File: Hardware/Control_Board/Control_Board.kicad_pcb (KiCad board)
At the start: 2 copper layers, 129.5 x 130.8 mm, 18 parts, among them J2 Term_01x02, J22 Conn_02x20_Odd_Even, J7 Term_01x02, K2 ALQ3F12

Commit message: PCB layout additions
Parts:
- added J**: 172447-YY02, Samacsys:172447-YY02, F.Cu at (45.7, 48.3)
- added J**: 172447-YY02, Samacsys:172447-YY02, F.Cu at (45.7, 55.9)
- added J**: 172447-YY02, Samacsys:172447-YY02, F.Cu at (45.7, 71.1)
- added J**: 172447-YY02, Samacsys:172447-YY02, F.Cu at (45.7, 63.5)
- D2 (x4): value LED -> LED_Red_power
- J2: value Term_01x02 -> Screw_Terminal_01x02
- R5 (x4): value 2k -> 10k
- moved D2 29.2 mm to (123.4, 124.4)
- moved J2 29.2 mm to (151.8, 141.6)
- moved J7 29.2 mm to (151.8, 127.6)
- moved J7 29.2 mm to (152.2, 88.9)
- moved K2 29.2 mm to (125.7, 128.9)
- moved K2 29.2 mm to (126.1, 102.9)
- moved R5 29.2 mm to (123.4, 108.0)
- moved K2 29.2 mm to (126.1, 90.2)
- moved D2 29.2 mm to (123.4, 111.1)
- moved D2 29.2 mm to (123.9, 85.7)
- moved D2 29.2 mm to (123.9, 98.4)
- moved J7 29.2 mm to (152.2, 101.6)
- moved J7 29.2 mm to (151.8, 114.3)
- moved K2 29.2 mm to (125.7, 115.6)
- moved R5 29.2 mm to (123.9, 95.2)
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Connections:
- D2 pad 1: (no net) -> Net-(D2-Pad1) (x4)
- D2 pad 2: (no net) -> +5V (x4)
- J2 pad 1: (no net) -> +12V
- J2 pad 2: (no net) -> +12V
- J7 pad 1: (no net) -> Net-(J7-Pad1) (x4)
- J7 pad 2: (no net) -> Net-(J7-Pad1) (x4)
- K2 pad 1: (no net) -> 12V (x4)
- K2 pad 2: (no net) -> Relay2 (x4)
- K2 pad 3: (no net) -> Net-(J5-Pad1) (x4)
- K2 pad 4: (no net) -> 120V_Hot (x4)
- R5 pad 1: (no net) -> GND (x4)
- R5 pad 2: (no net) -> Net-(R4-Pad1) (x4)
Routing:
- net (no net): track 12.8 -> 2.63 mm
- net GND: track 0.00 -> 8.65 mm
- net Net-(R4-Pad1): track 0.00 -> 1.56 mm
- added copper zone on B.Cu, net 120V_Hot
- added copper zone on F.Cu, net 120V_Hot
- added copper zone on B.Cu, net Net-(J7-Pad1)
- added copper zone on F.Cu, net Net-(J7-Pad1)
- removed copper zone on B.Cu, net (none)
- removed copper zone on F.Cu, net (none)
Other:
- outline, holes or cut-outs redrawn

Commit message: Control_Board updates
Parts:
- removed the D2 at (123.4, 111.1)
- removed the D2 at (123.9, 85.7)
- removed the D2 at (123.4, 124.4)
- removed the D2 at (123.9, 98.4)
- removed J** (x4): 172447-YY02, Samacsys:172447-YY02
- removed J22: Conn_02x20_Odd_Even, Connector_PinSocket_2.54mm:PinSocket_2x20_P2.54mm_Vertical
- removed the R5 at (123.4, 108.0)
- removed the R5 at (123.9, 95.2)
- removed the R5 at (123.4, 121.3)
- removed the R5 at (123.9, 82.5)
- added A1: Arduino_Nano_v3.x, Module:Arduino_Nano, F.Cu at (47.0, 78.7)
- added C1: 10uF, Capacitor_SMD:C_1206_3216Metric, F.Cu at (203.4, 63.2)
- added C2: 10uF, Capacitor_SMD:C_1206_3216Metric, F.Cu at (207.5, 61.7)
- added C3: 100nF, Capacitor_SMD:C_0603_1608Metric, F.Cu at (203.4, 57.7)
- added C4: 22uF, Capacitor_SMD:C_1206_3216Metric, F.Cu at (211.8, 55.4)
- added C5: 22uF, Capacitor_SMD:C_1206_3216Metric, F.Cu at (211.8, 53.0)
- added D1: LED_Red_power, LED_SMD:LED_0603_1608Metric, F.Cu at (195.8, 55.7)
- added D2: LED_Red_power, LED_SMD:LED_0603_1608Metric, F.Cu at (211.3, 63.0)
- added J1: Raspberry_Pi_2_3, Library Loader:HDRV40W64P254_2X20_5080X500X884P, F.Cu at (89.2, 75.2)
- added J7: 12V PWR IN, 1792863-2term_power:1792863, F.Cu at (44.2, 44.5)
- added L1: 3.3uH, Inductor_SMD:L_10.4x10.4_H4.8, F.Cu at (203.5, 49.0)
- added Q1: PMOS, Package_SO:SOIC-8_3.9x4.9mm_P1.27mm, F.Cu at (196.7, 59.3)
- added Q2: Q_Dual_PMOS_S1G1S2G2D2D2D1D1, Package_SO:SOP-8_3.9x4.9mm_P1.27mm, F.Cu at (212.6, 59.4)
- added R1: 10k, Resistor_SMD:R_0402_1005Metric_Pad0.72x0.64mm_HandSolder, F.Cu at (44.7, 76.9)
- added R2: 20k, Resistor_SMD:R_0402_1005Metric_Pad0.72x0.64mm_HandSolder, F.Cu at (43.9, 78.7)
- added R3: 10k, Resistor_SMD:R_0402_1005Metric, F.Cu at (198.4, 55.6)
- added R4: 56.2k, Resistor_SMD:R_0402_1005Metric, F.Cu at (208.0, 56.1)
- added R5: 10k, Resistor_SMD:R_0402_1005Metric, F.Cu at (208.0, 58.2)
- added R6: 6.8k, Resistor_SMD:R_0402_1005Metric, F.Cu at (214.1, 63.0)
- added R7: 6.8k, Resistor_SMD:R_0402_1005Metric, F.Cu at (214.1, 64.0)
- added U1: ULN2003, Package_SO:SOIC-16_3.9x9.9mm_P1.27mm, F.Cu at (116.8, 102.9)
- added U2: ULN2003, Package_SO:SOIC-16_3.9x9.9mm_P1.27mm, F.Cu at (118.1, 66.0)
- added U3: TPS563200, Package_TO_SOT_SMD:SOT-23-6, F.Cu at (203.3, 60.3)
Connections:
- K2 pad 1: 12V -> +12V (x4)
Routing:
- net U2/Pin1: track 0.00 -> 69.6 mm
- net U2/Pin3: track 0.00 -> 45.4 mm
- net Relay2: track 0.00 -> 44.0 mm
- net U2/Pin4: track 0.00 -> 42.8 mm
- net U2/Pin2: track 0.00 -> 38.0 mm
- net U1/Pin3: track 0.00 -> 33.5 mm, vias 0 -> 1
- net U1/Pin4: track 0.00 -> 33.2 mm, vias 0 -> 1
- net U1/Pin1: track 0.00 -> 23.9 mm, vias 0 -> 1
- net U1/Pin2: track 0.00 -> 23.0 mm, vias 0 -> 1
- net Relay1: track 0.00 -> 19.9 mm
- net GND: track 8.65 -> 0.00 mm
- net (no net): track 2.63 -> 0.00 mm
- net Net-(R4-Pad1): track 1.56 -> 0.00 mm
- added copper zone on F.Cu, net +12V
- added copper zone on B.Cu, net GND
- removed copper zone on F.Cu, net 120V_Hot
- removed copper zone on F.Cu, net Net-(J7-Pad1)
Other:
- outline, holes or cut-outs redrawn
- board text removed: "Relay 2"

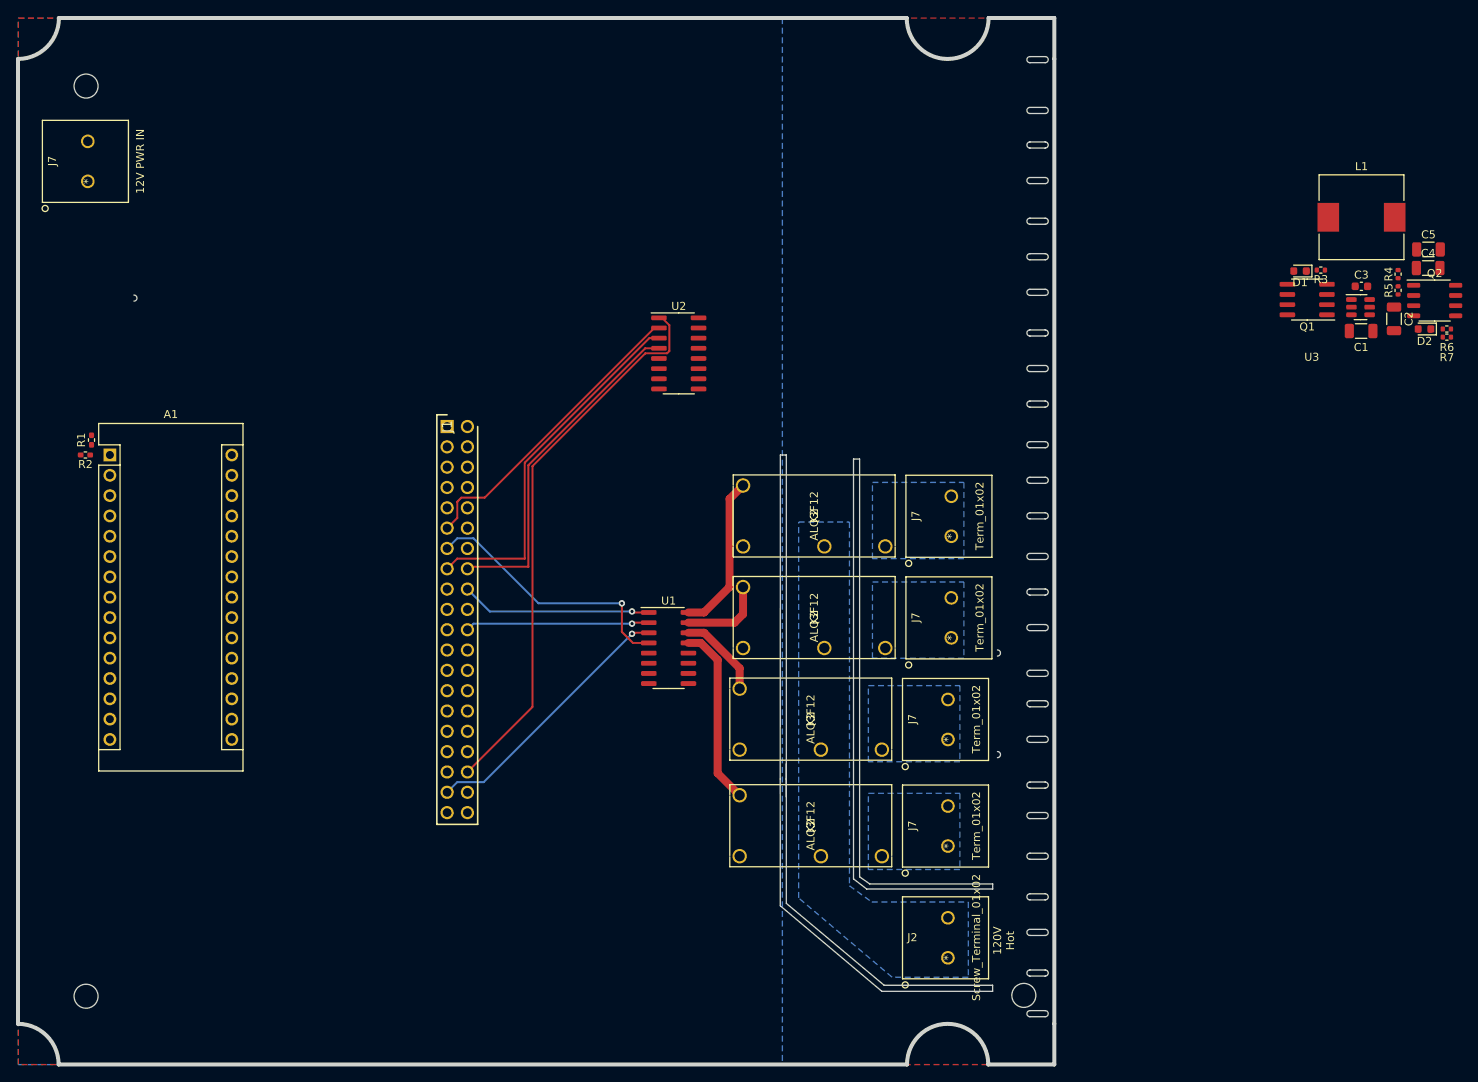
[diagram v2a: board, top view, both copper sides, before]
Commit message: Board updates, ready for power regulation component placements
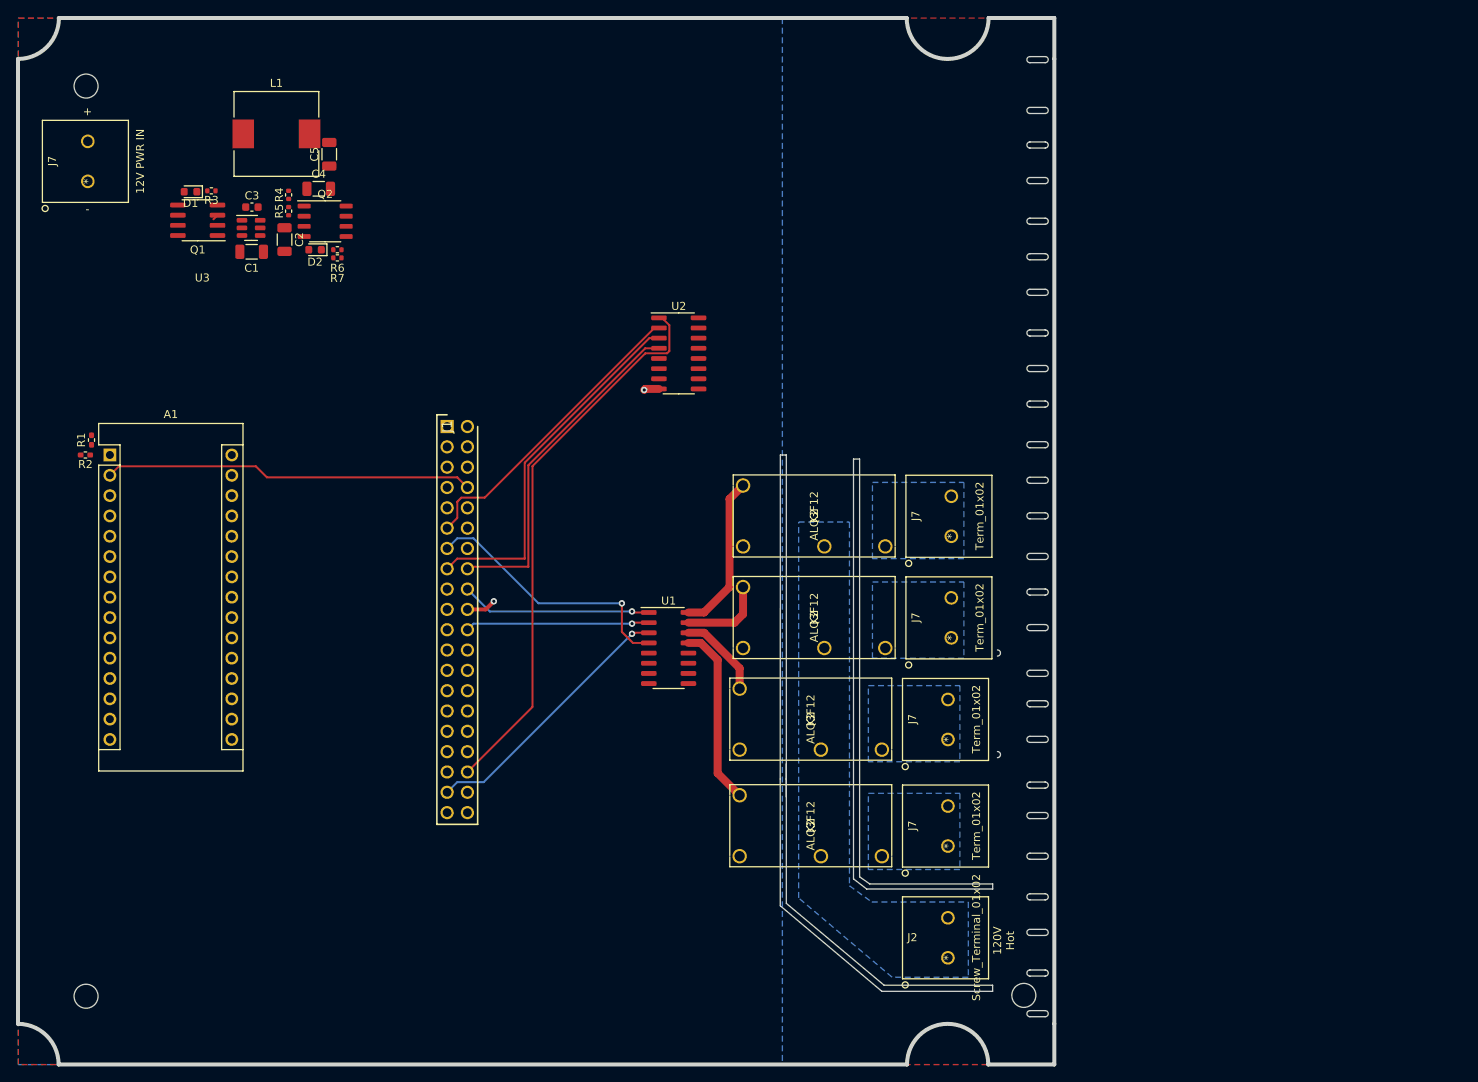
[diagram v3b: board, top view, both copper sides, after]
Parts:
- moved C4 139.0 mm to (73.1, 45.5)
- moved Q2 139.0 mm to (73.9, 49.5)
- moved R4 139.0 mm to (69.3, 46.2)
- moved R5 139.0 mm to (69.3, 48.3)
- moved R6 139.0 mm to (75.4, 53.1)
- moved R7 139.0 mm to (75.4, 54.1)
- moved U3 139.0 mm to (64.6, 50.4)
- moved C1 139.0 mm to (64.7, 53.3)
- moved C2 139.0 mm to (68.8, 51.8)
- moved C3 139.0 mm to (64.8, 47.8)
- moved D1 139.0 mm to (57.1, 45.8)
- moved D2 139.0 mm to (72.6, 53.1)
- moved Q1 139.0 mm to (58.0, 49.4)
- moved R3 139.0 mm to (59.7, 45.7)
- moved C5 137.9 mm to (74.4, 41.1), turned to 90 degrees
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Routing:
- net TX: track 0.00 -> 46.3 mm
- net GND: track 0.00 -> 5.62 mm, vias 0 -> 2
- net Net-(C1-Pad1): track 0.00 -> 0.72 mm
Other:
- outline, holes or cut-outs redrawn
- board text added: "+"
- board text added: "-"

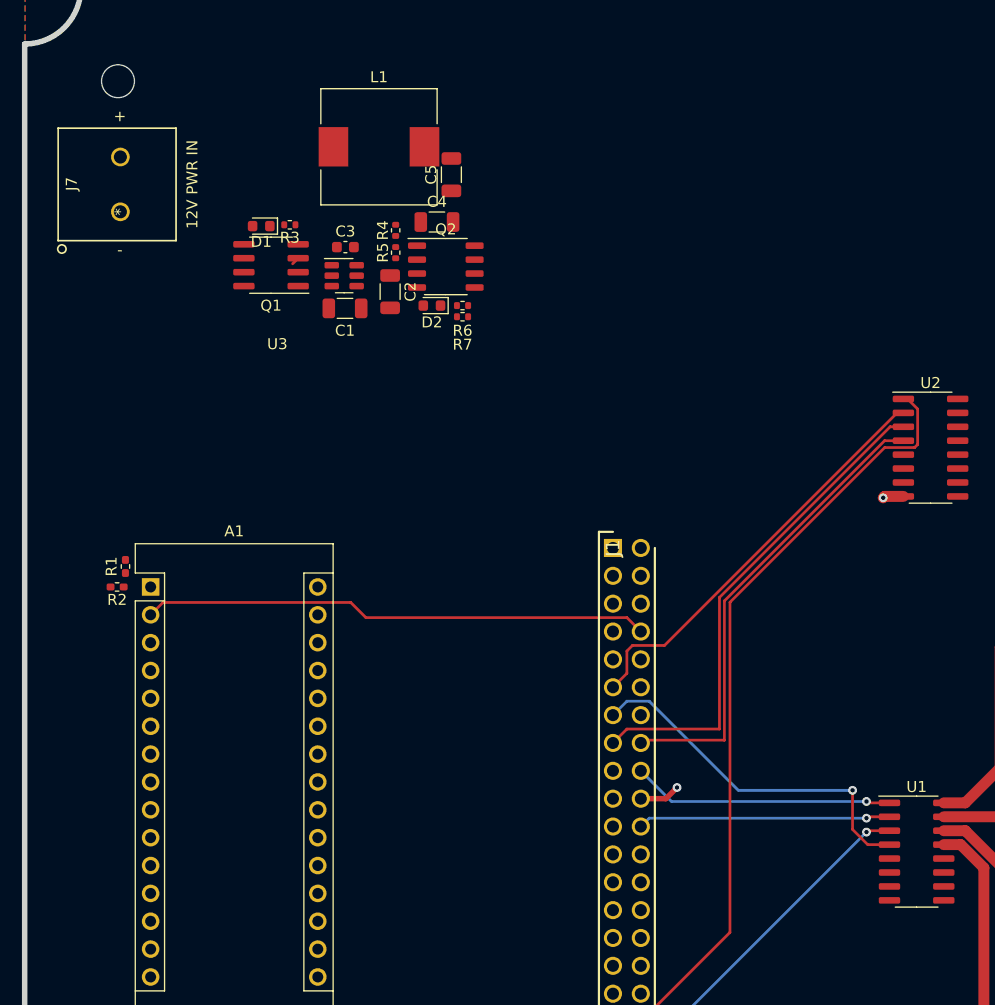
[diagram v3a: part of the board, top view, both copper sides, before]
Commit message: Laid out power regulation stuffs
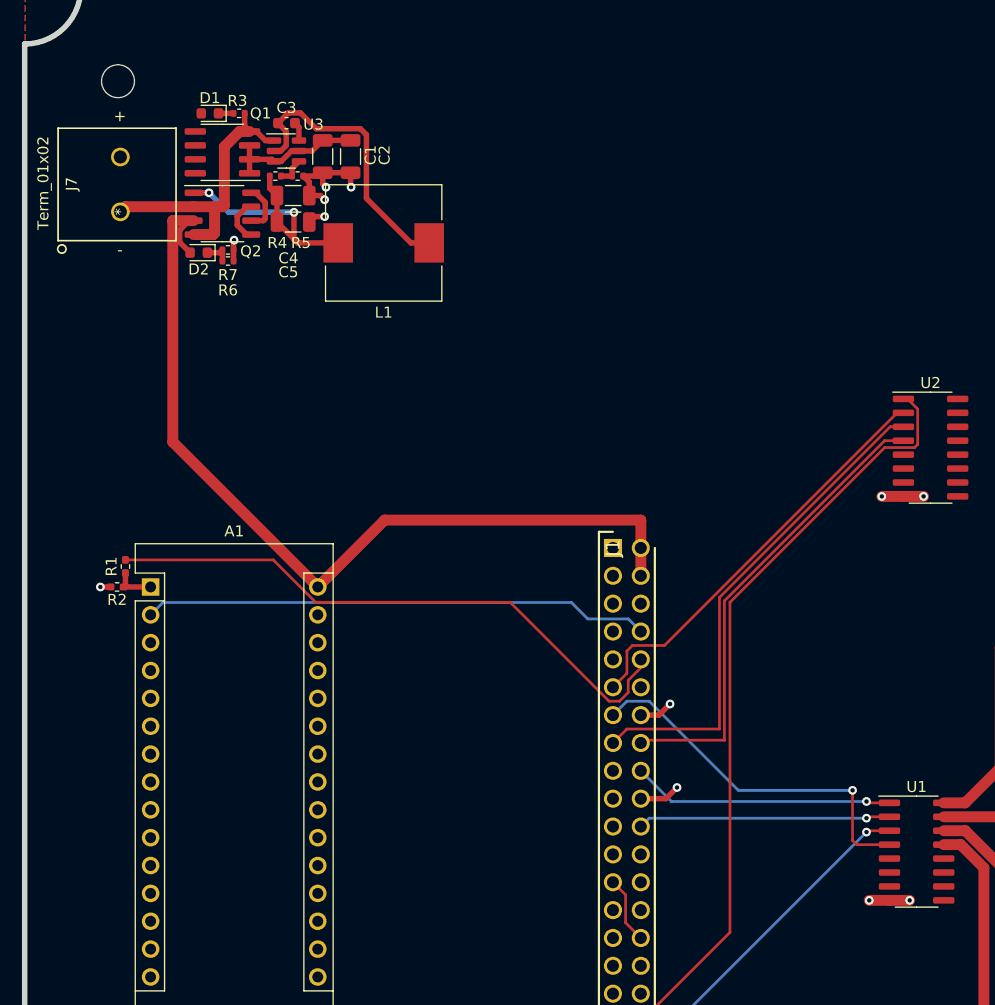
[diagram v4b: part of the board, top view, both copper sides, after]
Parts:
- J7: value 12V PWR IN -> Term_01x02
- moved R7 22.2 mm to (54.1, 48.0)
- moved D2 21.8 mm to (51.4, 48.3)
- moved R6 21.8 mm to (54.1, 49.0)
- moved Q2 20.9 mm to (53.5, 44.7)
- moved C5 15.1 mm to (60.0, 45.5), turned to 0 degrees
- moved C1 14.0 mm to (62.7, 39.5), turned to -90 degrees
- moved C4 13.3 mm to (60.0, 43.1)
- moved C2 12.8 mm to (65.2, 39.5)
- moved U3 12.5 mm to (59.4, 39.0)
- moved C3 12.5 mm to (59.4, 36.4)
- moved R4 12.0 mm to (58.4, 41.3), turned to 180 degrees
- moved R5 11.3 mm to (60.4, 41.3), turned to 180 degrees
- moved D1 11.3 mm to (52.4, 35.6)
- moved Q1 11.2 mm to (53.5, 39.1)
- moved R3 11.2 mm to (55.1, 35.6)
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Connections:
- J7 pad 1: GND -> Net-(J7-Pad1)
- J7 pad 2: +12V -> Net-(J7-Pad1)
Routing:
- net +5V: track 0.00 -> 81.9 mm
- net GND: track 5.62 -> 62.4 mm, vias 2 -> 12
- net Net-(J1-Pad10): track 0.00 -> 55.0 mm
- net Net-(C3-Pad1): track 0.00 -> 26.1 mm
- net Net-(C4-Pad1): track 0.00 -> 23.7 mm, vias 0 -> 2
- net Relay2: track 44.0 -> 63.9 mm
- net Relay1: track 19.9 -> 0.00 mm
- net Net-(C1-Pad1): track 0.72 -> 12.6 mm
- net Net-(Q2-Pad6): track 0.00 -> 4.48 mm
- net Net-(Q2-Pad5): track 0.00 -> 4.08 mm
- net RX: track 0.00 -> 3.80 mm
- net Net-(R4-Pad1): track 0.00 -> 2.61 mm
- net Net-(D2-Pad1): track 0.00 -> 2.49 mm
- net Net-(C3-Pad2): track 0.00 -> 1.74 mm
- net Net-(D1-Pad1): track 0.00 -> 1.37 mm
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
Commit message: 10_23_2022_3_pin_headers
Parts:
- added A0: HDRV3W64P0X254_1X3_762X254X864P, Library:HDRV3W64P0X254_1X3_762X254X864P, F.Cu at (67.9, 110.6)
- added A1: HDRV3W64P0X254_1X3_762X254X864P, Library:HDRV3W64P0X254_1X3_762X254X864P, F.Cu at (67.9, 105.0)
- added A2: HDRV3W64P0X254_1X3_762X254X864P, Library:HDRV3W64P0X254_1X3_762X254X864P, F.Cu at (67.7, 99.1)
- added A3: HDRV3W64P0X254_1X3_762X254X864P, Library:HDRV3W64P0X254_1X3_762X254X864P, F.Cu at (67.7, 93.3)
- added A4: HDRV3W64P0X254_1X3_762X254X864P, Library:HDRV3W64P0X254_1X3_762X254X864P, F.Cu at (67.4, 87.4)
- added T/H: HDRV3W64P0X254_1X3_762X254X864P, Library:HDRV3W64P0X254_1X3_762X254X864P, F.Cu at (80.1, 76.5)
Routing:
- net +5V: track 81.9 -> 193.2 mm
- net Net-(J1-Pad10): track 55.0 -> 41.5 mm
- net A4: track 0.00 -> 12.3 mm
- net A0: track 0.00 -> 11.1 mm
- net A3: track 0.00 -> 10.4 mm
- net A1: track 0.00 -> 9.57 mm
- net unconnected-(J1-Pad7): track 0.00 -> 9.13 mm
- net A2: track 0.00 -> 9.04 mm
- net GND: track 62.4 -> 64.0 mm
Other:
- board text added: "5V"
- board text added: "GND"
- board text added: "GPIO4"
- board text added: "S"

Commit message: Updated Analog sensor routing
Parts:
- moved T/H 14.1 mm to (72.1, 64.8)
- moved A4 3.02 mm to (68.6, 90.2)
- moved A3 2.10 mm to (68.6, 95.2)
- moved A2 1.55 mm to (68.6, 100.3)
- moved A1 0.74 mm to (68.6, 105.4)
- moved A0 0.65 mm to (68.6, 110.5)
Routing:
- net +5V: track 193.2 -> 124.7 mm
- net Relay2: track 63.9 -> 10.7 mm
- net Net-(J1-Pad10): track 41.5 -> 56.9 mm, vias 0 -> 1
- net unconnected-(J1-Pad7): track 9.13 -> 24.3 mm
- net GND: track 64.0 -> 55.5 mm
- net A2: track 9.04 -> 10.3 mm
- net A1: track 9.57 -> 10.8 mm
- net A3: track 10.4 -> 11.1 mm
- net TX: track 46.3 -> 47.0 mm
- net A4: track 12.3 -> 13.0 mm
- net A0: track 11.1 -> 11.7 mm

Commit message: v0.1 Ready for review
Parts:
- removed J7 (x5): Term_01x02, 1792863-2term_power:1792863
- removed the K2 at (125.7, 128.9)
- removed the K2 at (126.1, 102.9)
- removed the K2 at (126.1, 90.2)
- removed the K2 at (125.7, 115.6)
- added J**: 197054301, Samacsys:197054301, F.Cu at (139.7, 64.8)
- added J**: 197054301, Samacsys:197054301, F.Cu at (152.1, 58.4)
- added J**: 197054301, Samacsys:197054301, F.Cu at (139.7, 52.1)
- added J**: 197054301, Samacsys:197054301, F.Cu at (152.1, 71.1)
- added J**: 197054301, Samacsys:197054301, F.Cu at (152.1, 64.8)
- added J**: 197054301, Samacsys:197054301, F.Cu at (139.7, 58.4)
- added J**: 197054301, Samacsys:197054301, F.Cu at (152.1, 52.1)
- added J**: 197054301, Samacsys:197054301, F.Cu at (139.7, 71.1)
- added J112: 19705-4301, Samacsys:197054301, F.Cu at (151.1, 128.3)
- added J3: Screw_Terminal_01x02, Samacsys:197054301, F.Cu at (40.6, 45.1)
- added J4: 19705-4301, Samacsys:197054301, F.Cu at (151.8, 89.5)
- added J5: 19705-4301, Samacsys:197054301, F.Cu at (151.1, 101.6)
- added J6: 19705-4301, Samacsys:197054301, F.Cu at (151.1, 114.9)
- added J8: 19705-4301, Samacsys:197054301, F.Cu at (151.1, 141.6)
- added K1: ALQ3F12, Samacsys:G5Q1A4DC24, F.Cu at (126.2, 90.3)
- added K2: ALQ3F12, Samacsys:G5Q1A4DC24, F.Cu at (126.2, 103.0)
- added K3: ALQ3F12, Samacsys:G5Q1A4DC24, F.Cu at (126.2, 115.7)
- added K4: ALQ3F12, Samacsys:G5Q1A4DC24, F.Cu at (126.2, 128.4)
- A1: value HDRV3W64P0X254_1X3_762X254X864P -> Arduino_Nano_v3.x
- J2: footprint 1792863-2term_power:1792863 -> Samacsys:197054301
- moved J2 150.9 mm to (40.6, 39.4), turned to 0 degrees
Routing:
- net Pump1: track 0.00 -> 23.1 mm
- net Relay4: track 0.00 -> 22.2 mm
- net Pump4: track 0.00 -> 21.5 mm
- net Pump2: track 0.00 -> 21.0 mm
- net Relay1: track 0.00 -> 19.7 mm
- net Pump3: track 0.00 -> 19.4 mm
- net Relay3: track 0.00 -> 12.0 mm
- net GND: track 55.5 -> 57.6 mm, vias 12 -> 15
- net Relay2: track 10.7 -> 8.62 mm
- added copper zone on B.Cu, net Net-(K1-Pad3)
- added copper zone on B.Cu, net Net-(K2-Pad3)
- added copper zone on B.Cu, net Net-(K3-Pad3)
- added copper zone on B.Cu, net Net-(K4-Pad3)
- removed copper zone on B.Cu, net Net-(J7-Pad1)
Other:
- outline, holes or cut-outs redrawn
- board text added: "Vertial Farm Controller v0.1"

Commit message: Vertical fix
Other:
- board text added: "Vertical Farm Controller v0.1"
- board text removed: "Vertial Farm Controller v0.1"
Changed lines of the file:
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@@
     (effects (font (size 1 1) (thickness 0.25)))
   )
-  (gr_text "Vertial Farm Controller v0.1" (at 97.79 152.4) (layer "F.SilkS")
+  (gr_text "Vertical Farm Controller v0.1" (at 97.79 152.4) (layer "F.SilkS")
     (effects (font (size 2.54 2.54) (thickness 0.3)))
   )
